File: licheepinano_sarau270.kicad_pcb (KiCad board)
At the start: 2 copper layers, 81.3 x 51.9 mm, 92 parts, among them Con1 SIM8050-6-0-14-01-A, Con2 WE-RJ45_7498011122AR, P1 RF2-03E-T-00-50-G, Q1 BC847B, Q2 BC847B, T1 FDN304P, U1 LAN9514I, U2 IP4220CZ6, U4 MAX-M8C, U5 TXB0104, X1 ABM3-25.000MHZ-D2Y-T

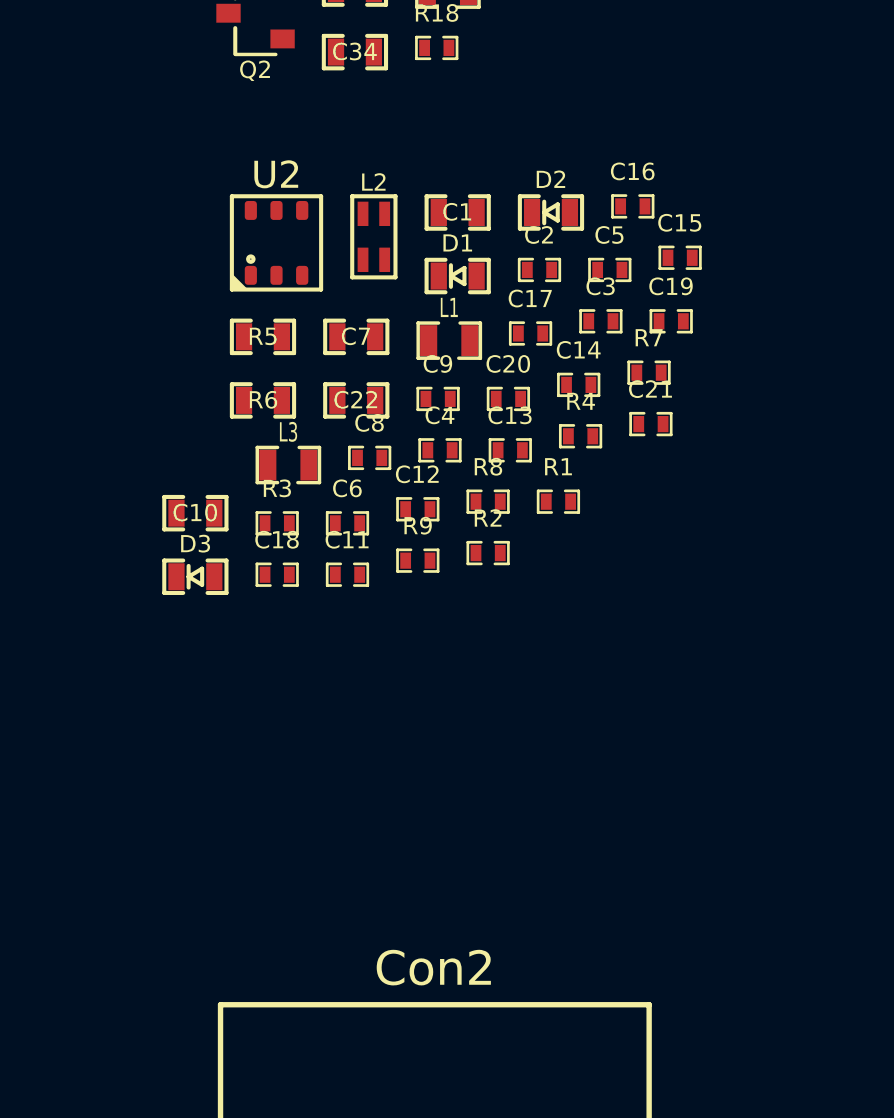
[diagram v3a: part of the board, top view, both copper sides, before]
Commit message: Added connection for ethernet modules
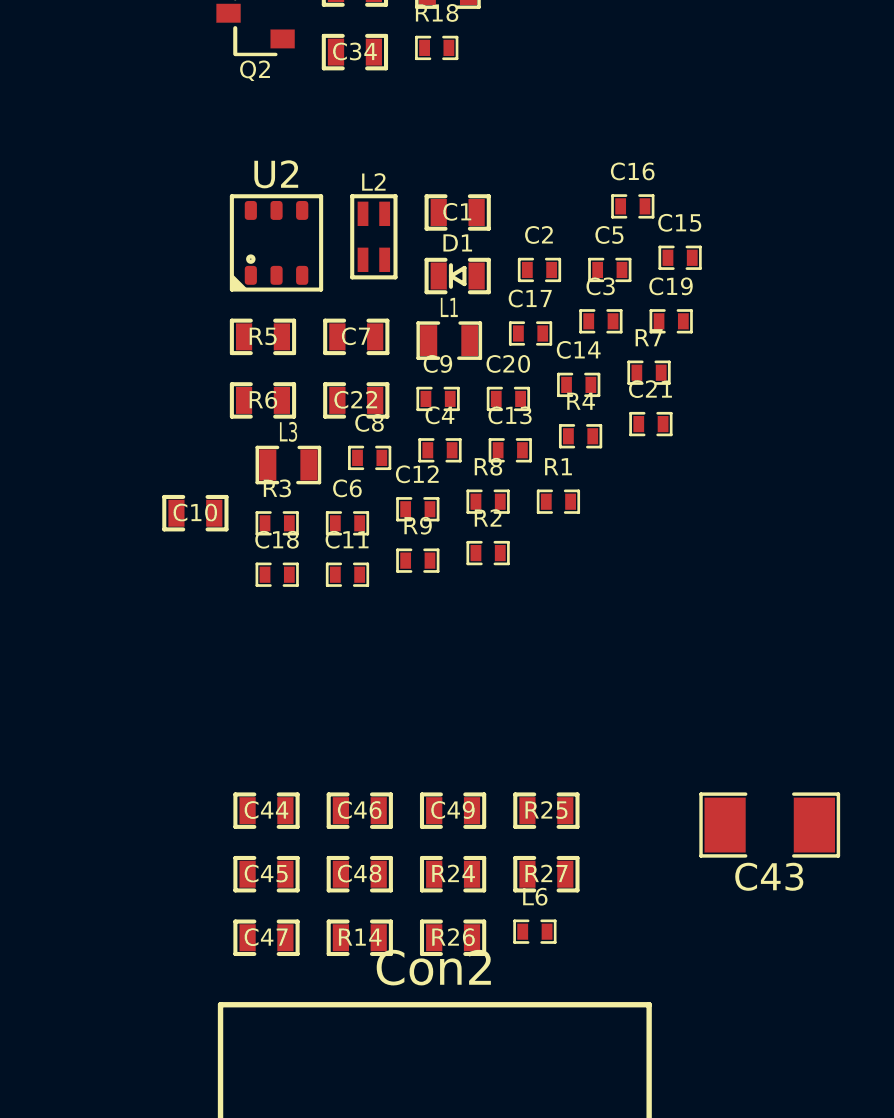
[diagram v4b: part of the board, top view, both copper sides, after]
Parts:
- removed D2: KPT-1608CGCK, Diodes:LED_KPT-1608CGCK
- removed D3: KP-1608YC, Diodes:LED_KP-1608YC
- added C43: 1nF/2kV, Capacitors_Smd_1206:1nF_2kV_1206, F.Cu at (213.7, 83.3)
- added C44: 15pF/50V, Capacitors_Smd_0603:15pF_0603, F.Cu at (195.0, 82.8)
- added C45: 15pF/50V, Capacitors_Smd_0603:15pF_0603, F.Cu at (195.0, 85.1)
- added C46: 15pF/50V, Capacitors_Smd_0603:15pF_0603, F.Cu at (198.5, 82.8)
- added C47: 15pF/50V, Capacitors_Smd_0603:15pF_0603, F.Cu at (195.0, 87.5)
- added C48: 22nF/50V, Capacitors_Smd_0603:22nF_0603, F.Cu at (198.5, 85.1)
- added C49: 22nF/50V, Capacitors_Smd_0603:22nF_0603, F.Cu at (201.9, 82.8)
- added L6: BLM15HG601SN1D, Inductors:BLM15HG601SN1D_0402, F.Cu at (205.0, 87.3)
- added R14: 49R9, Resistor_Smd_0603:49R9_0603, F.Cu at (198.5, 87.5)
- added R24: 49R9, Resistor_Smd_0603:49R9_0603, F.Cu at (201.9, 85.1)
- added R25: 49R9, Resistor_Smd_0603:49R9_0603, F.Cu at (205.4, 82.8)
- added R26: 49R9, Resistor_Smd_0603:49R9_0603, F.Cu at (201.9, 87.5)
- added R27: 10R/1%, Resistor_Smd_0603:10R_0603, F.Cu at (205.4, 85.1)
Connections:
- net /Modem 3G/MODEM_POWER_IN renamed 3V8
- C1 pad 1: /USB Hub Module/POWER_IN_3V3 -> 3V3
- C11 pad 1: /USB Hub Module/POWER_IN_3V3 -> 3V3
- C2 pad 1: /USB Hub Module/POWER_IN_3V3 -> 3V3
- C5 pad 1: /USB Hub Module/POWER_IN_3V3 -> 3V3
- C6 pad 1: /USB Hub Module/POWER_IN_3V3 -> 3V3
- C8 pad 1: /USB Hub Module/POWER_IN_3V3 -> 3V3
- Con2 pad 1: (no net) -> /USB Hub Module/ETHERNET_TXP
- Con2 pad 10: (no net) -> /Ethernet Connector Module/LED_Yellow_-
- Con2 pad 11: (no net) -> 3V3
- Con2 pad 12: (no net) -> /Ethernet Connector Module/LED_Green_-
- Con2 pad 2: (no net) -> Net-(C48-Pad1)
- Con2 pad 3: (no net) -> /USB Hub Module/ETHERNET_TXN
- Con2 pad 4: (no net) -> /USB Hub Module/ETHERNET_RXP
- Con2 pad 5: (no net) -> Net-(C48-Pad1)
- Con2 pad 6: (no net) -> /USB Hub Module/ETHERNET_RXN
- Con2 pad 9: (no net) -> 3V3
- Con2 pad Z1: (no net) -> /Ethernet Connector Module/SHIELD1
- Con2 pad Z2: (no net) -> /Ethernet Connector Module/SHIELD1
- L3 pad 2: /USB Hub Module/POWER_IN_3V3 -> 3V3
- R2 pad 2: /USB Hub Module/POWER_IN_3V3 -> 3V3
- R7 pad 1: /USB Hub Module/POWER_IN_3V3 -> 3V3
- R8 pad 1: /USB Hub Module/POWER_IN_3V3 -> /Ethernet Connector Module/LED_Green_-
- R8 pad 2: Net-(D2-Pad1) -> Net-(R8-Pad2)
- R9 pad 1: /USB Hub Module/POWER_IN_3V3 -> /Ethernet Connector Module/LED_Yellow_-
- R9 pad 2: Net-(D3-Pad1) -> Net-(R9-Pad2)
- U1 pad 11: /USB Hub Module/POWER_IN_3V3 -> 3V3
- U1 pad 19: /USB Hub Module/POWER_IN_3V3 -> 3V3
- U1 pad 21: Net-(D2-Pad2) -> Net-(R8-Pad2)
- U1 pad 22: Net-(D3-Pad2) -> Net-(R9-Pad2)
- U1 pad 27: /USB Hub Module/POWER_IN_3V3 -> 3V3
- U1 pad 33: /USB Hub Module/POWER_IN_3V3 -> 3V3
- U1 pad 39: /USB Hub Module/POWER_IN_3V3 -> 3V3
- U1 pad 40: /USB Hub Module/POWER_IN_3V3 -> 3V3
- U1 pad 46: /USB Hub Module/POWER_IN_3V3 -> 3V3
- U1 pad 52: (no net) -> /USB Hub Module/ETHERNET_RXP
- U1 pad 53: (no net) -> /USB Hub Module/ETHERNET_RXN
- U1 pad 55: (no net) -> /USB Hub Module/ETHERNET_TXP
- U1 pad 56: (no net) -> /USB Hub Module/ETHERNET_TXN

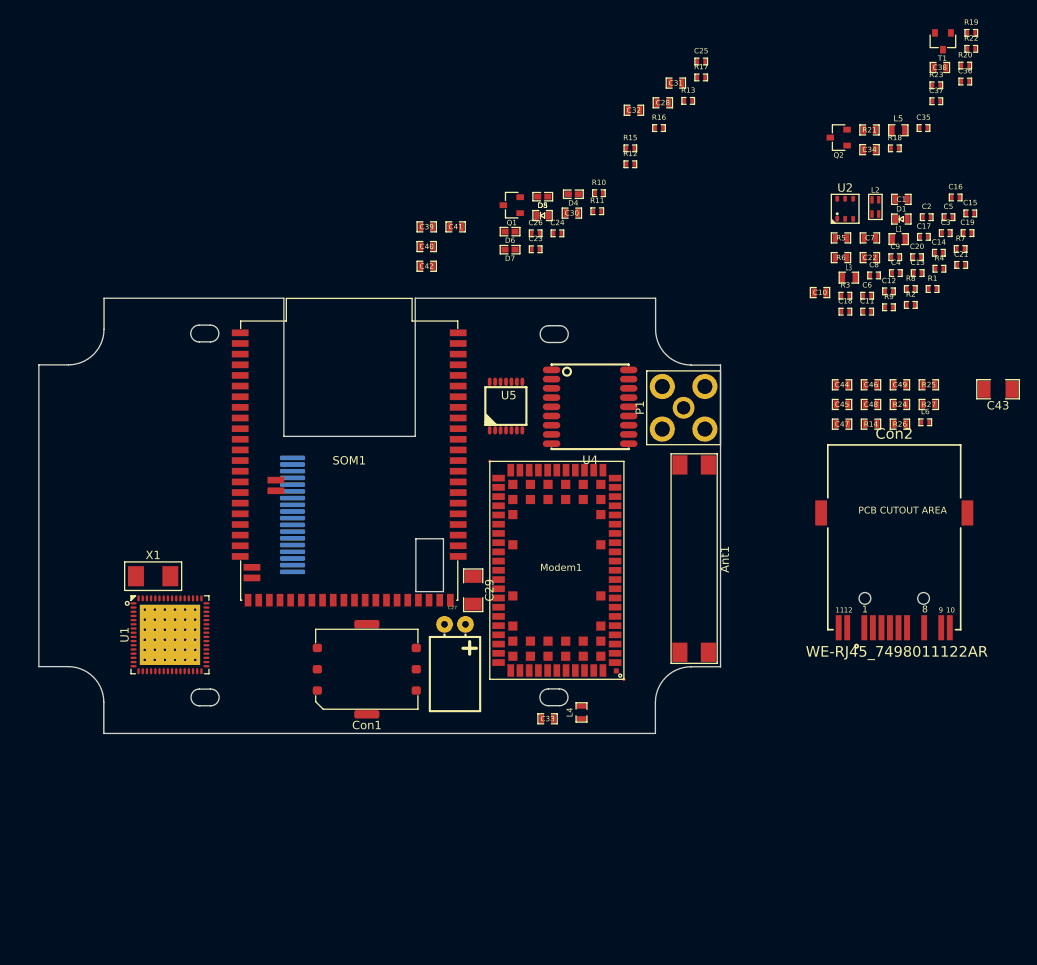
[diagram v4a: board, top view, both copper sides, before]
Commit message: Added WiFi and figurated some components on pcb
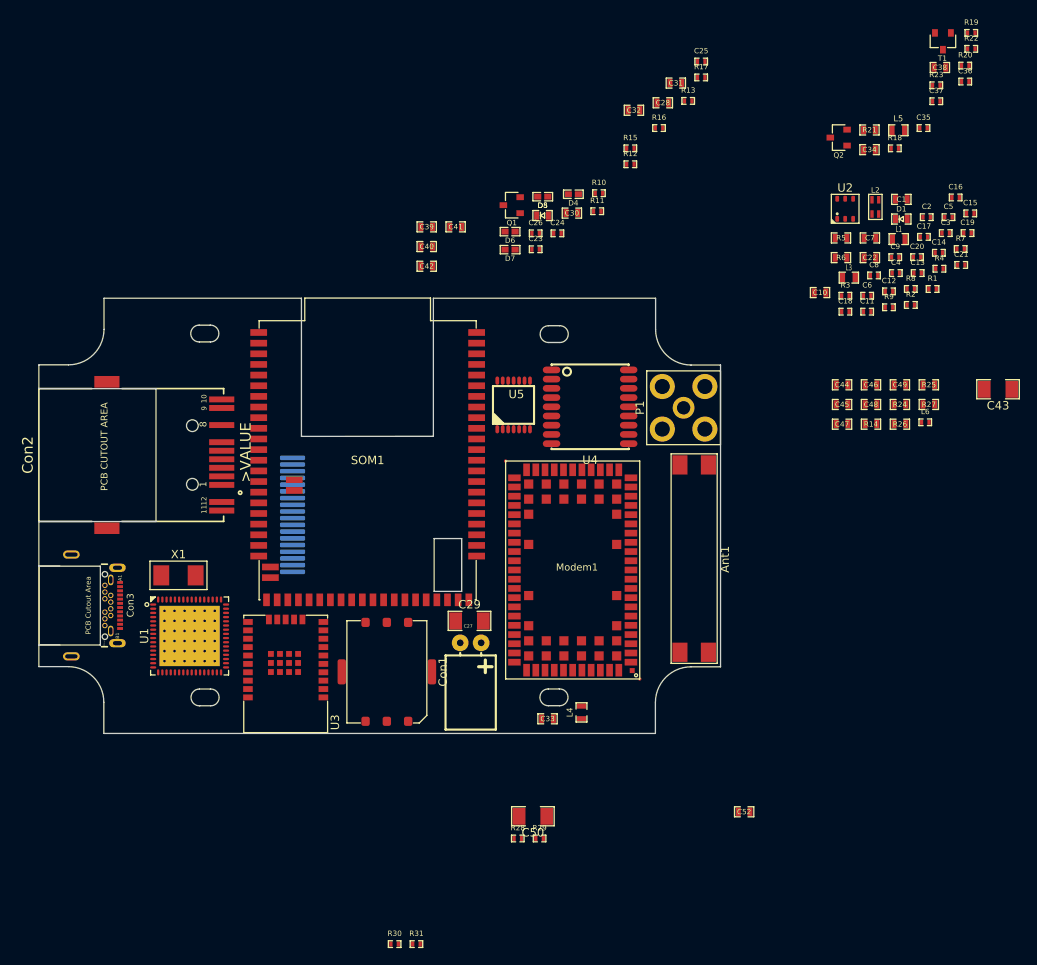
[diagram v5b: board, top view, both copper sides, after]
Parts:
- added C50: 1nF/2kV, Capacitors_Smd_1206:1nF_2kV_1206, F.Cu at (158.2, 134.2)
- added C52: 100nF/16V, Capacitors_Smd_0603:100nF_0603, F.Cu at (183.4, 133.7)
- added Con3: USB_C_Wurth_632723130112, Connector_USB:USB_C_632723130112, F.Cu at (104.3, 109.1)
- added R28: 0R, Resistor_Smd_0402:0R_0402, F.Cu at (156.4, 136.9)
- added R29: 0R, Resistor_Smd_0402:0R_0402, F.Cu at (159.0, 136.9)
- added R30: 0R, Resistor_Smd_0402:0R_0402, F.Cu at (141.7, 149.5)
- added R31: 0R, Resistor_Smd_0402:0R_0402, F.Cu at (144.3, 149.5)
- added U3: LILY-W132, UBlox_WiFi_Module:LILY_W132, F.Cu at (128.7, 117.3)
- Con2: value WE-RJ45_7498011122AR -> >VALUE
- moved Con2 85.5 mm to (117.5, 91.2), turned to 90 degrees
- moved C29 3.68 mm to (150.6, 110.9), turned to 180 degrees
- moved X1 3.02 mm to (115.9, 105.5)
- moved C27 2.89 mm to (150.7, 113.6)
- moved Con1 2.41 mm to (140.7, 117.0), turned to 270 degrees
- moved U1 2.34 mm to (117.2, 112.7)
- moved SOM1 2.20 mm to (138.4, 91.8)
- moved Modem1 1.89 mm to (162.9, 104.9)
- moved U5 0.92 mm to (155.8, 85.2)
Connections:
- C15 pad 1: /USB Hub Module/VDD_PHY -> /Ethernet Connector Module/POWER_IN_3V3
- C16 pad 1: /USB Hub Module/VDD_PHY -> /Ethernet Connector Module/POWER_IN_3V3
- C17 pad 1: /USB Hub Module/VDD_PHY -> /Ethernet Connector Module/POWER_IN_3V3
- C18 pad 1: /USB Hub Module/VDD_PHY -> /Ethernet Connector Module/POWER_IN_3V3
- C19 pad 1: /USB Hub Module/VDD_PHY -> /Ethernet Connector Module/POWER_IN_3V3
- C20 pad 1: /USB Hub Module/VDD_PHY -> /Ethernet Connector Module/POWER_IN_3V3
- C21 pad 1: /USB Hub Module/VDD_PHY -> /Ethernet Connector Module/POWER_IN_3V3
- DIS1 pad 10: (no net) -> /LCD Module/LED_A
- DIS1 pad 11: (no net) -> /LCD Module/LED_K1
- DIS1 pad 12: (no net) -> /LCD Module/LED_K1
- DIS1 pad 13: (no net) -> /LCD Module/LED_K1
- DIS1 pad 14: (no net) -> /LCD Module/LED_K1
- DIS1 pad 15: (no net) -> /LicheePi Nano SOM/TPX2
- DIS1 pad 16: (no net) -> /LicheePi Nano SOM/TPY2
- DIS1 pad 17: (no net) -> /LicheePi Nano SOM/TPX1
- DIS1 pad 18: (no net) -> /LicheePi Nano SOM/TPY1
- DIS1 pad 3: (no net) -> /LCD Module/CLK
- DIS1 pad 5: (no net) -> /LCD Module/CS
- DIS1 pad 6: (no net) -> /LCD Module/MOSI
- DIS1 pad 7: (no net) -> /LCD Module/MISO
- L3 pad 1: /USB Hub Module/VDD_PHY -> /Ethernet Connector Module/POWER_IN_3V3
- L6 pad 1: 3V3 -> /Ethernet Connector Module/POWER_IN_3V3
- Modem1 pad 2: /Modem 3G/GPS_V_BCKP -> /GPS Module/GPS_V_BCKP
- R13 pad 1: /Modem 3G/GPS_V_BCKP -> /GPS Module/GPS_V_BCKP
- SOM1 pad 1: (no net) -> /LCD Module/MISO
- SOM1 pad 10: (no net) -> /Logic Voltage Shifter/SIG1_HIGH_PART
- SOM1 pad 11: (no net) -> /Logic Voltage Shifter/SIG3_HIGH_PART
- SOM1 pad 12: (no net) -> /Logic Voltage Shifter/SIG2_HIGH_PART
- SOM1 pad 15: (no net) -> /Logic Voltage Shifter/SIG4_HIGH_PART
- SOM1 pad 3: (no net) -> /LCD Module/MOSI
- SOM1 pad 45: (no net) -> /LicheePi Nano SOM/TPY2
- SOM1 pad 47: (no net) -> /LicheePi Nano SOM/TPY1
- SOM1 pad 49: (no net) -> /LicheePi Nano SOM/TPX2
- SOM1 pad 5: (no net) -> /LCD Module/CS
- SOM1 pad 51: (no net) -> /LicheePi Nano SOM/TPX1
- SOM1 pad 53: (no net) -> 3V3
- SOM1 pad 55: (no net) -> GND
- SOM1 pad 57: (no net) -> /LicheePi Nano SOM/POWER_IN_5V0
- SOM1 pad 62: (no net) -> /LicheePi Nano SOM/USB_D_P
- SOM1 pad 64: (no net) -> /LicheePi Nano SOM/USB_D_N
- SOM1 pad 65: (no net) -> /LCD Module/LED_A
- SOM1 pad 66: (no net) -> /LCD Module/LED_K1
- SOM1 pad 7: (no net) -> /LCD Module/CLK
- U1 pad 10: /USB Hub Module/VDD_PHY -> /Ethernet Connector Module/POWER_IN_3V3
- U1 pad 3: (no net) -> /USB Hub Module/USB_D3_OUT_N
- U1 pad 4: (no net) -> /USB Hub Module/USB_D3_OUT_P
- U1 pad 49: /USB Hub Module/VDD_PHY -> /Ethernet Connector Module/POWER_IN_3V3
- U1 pad 5: /USB Hub Module/VDD_PHY -> /Ethernet Connector Module/POWER_IN_3V3
- U1 pad 51: /USB Hub Module/VDD_PHY -> /Ethernet Connector Module/POWER_IN_3V3
- U1 pad 54: /USB Hub Module/VDD_PHY -> /Ethernet Connector Module/POWER_IN_3V3
- U1 pad 57: /USB Hub Module/VDD_PHY -> /Ethernet Connector Module/POWER_IN_3V3
- U1 pad 58: (no net) -> /LicheePi Nano SOM/USB_D_N
- U1 pad 59: (no net) -> /LicheePi Nano SOM/USB_D_P
- U1 pad 64: /USB Hub Module/VDD_PHY -> /Ethernet Connector Module/POWER_IN_3V3
- U5 pad 2: (no net) -> /Logic Voltage Shifter/SIG1_HIGH_PART
- U5 pad 3: (no net) -> /Logic Voltage Shifter/SIG2_HIGH_PART
- U5 pad 4: (no net) -> /Logic Voltage Shifter/SIG3_HIGH_PART
- U5 pad 5: (no net) -> /Logic Voltage Shifter/SIG4_HIGH_PART
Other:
- outline, holes or cut-outs redrawn
